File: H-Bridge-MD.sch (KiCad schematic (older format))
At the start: 67 parts, among them IC1 SI8650AB-B-IS1, IC2 A3921KLPTR-T, IC3 SI8650AB-B-IS1, IC4 A3921KLPTR-T, J1 Conn_01x02, J2 Conn_01x03, J3 Conn_01x05, J4 Conn_01x02, J5 Bus_mechaken_PCIexpress_x16_1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, Q1 NVMFD5C446NT1G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

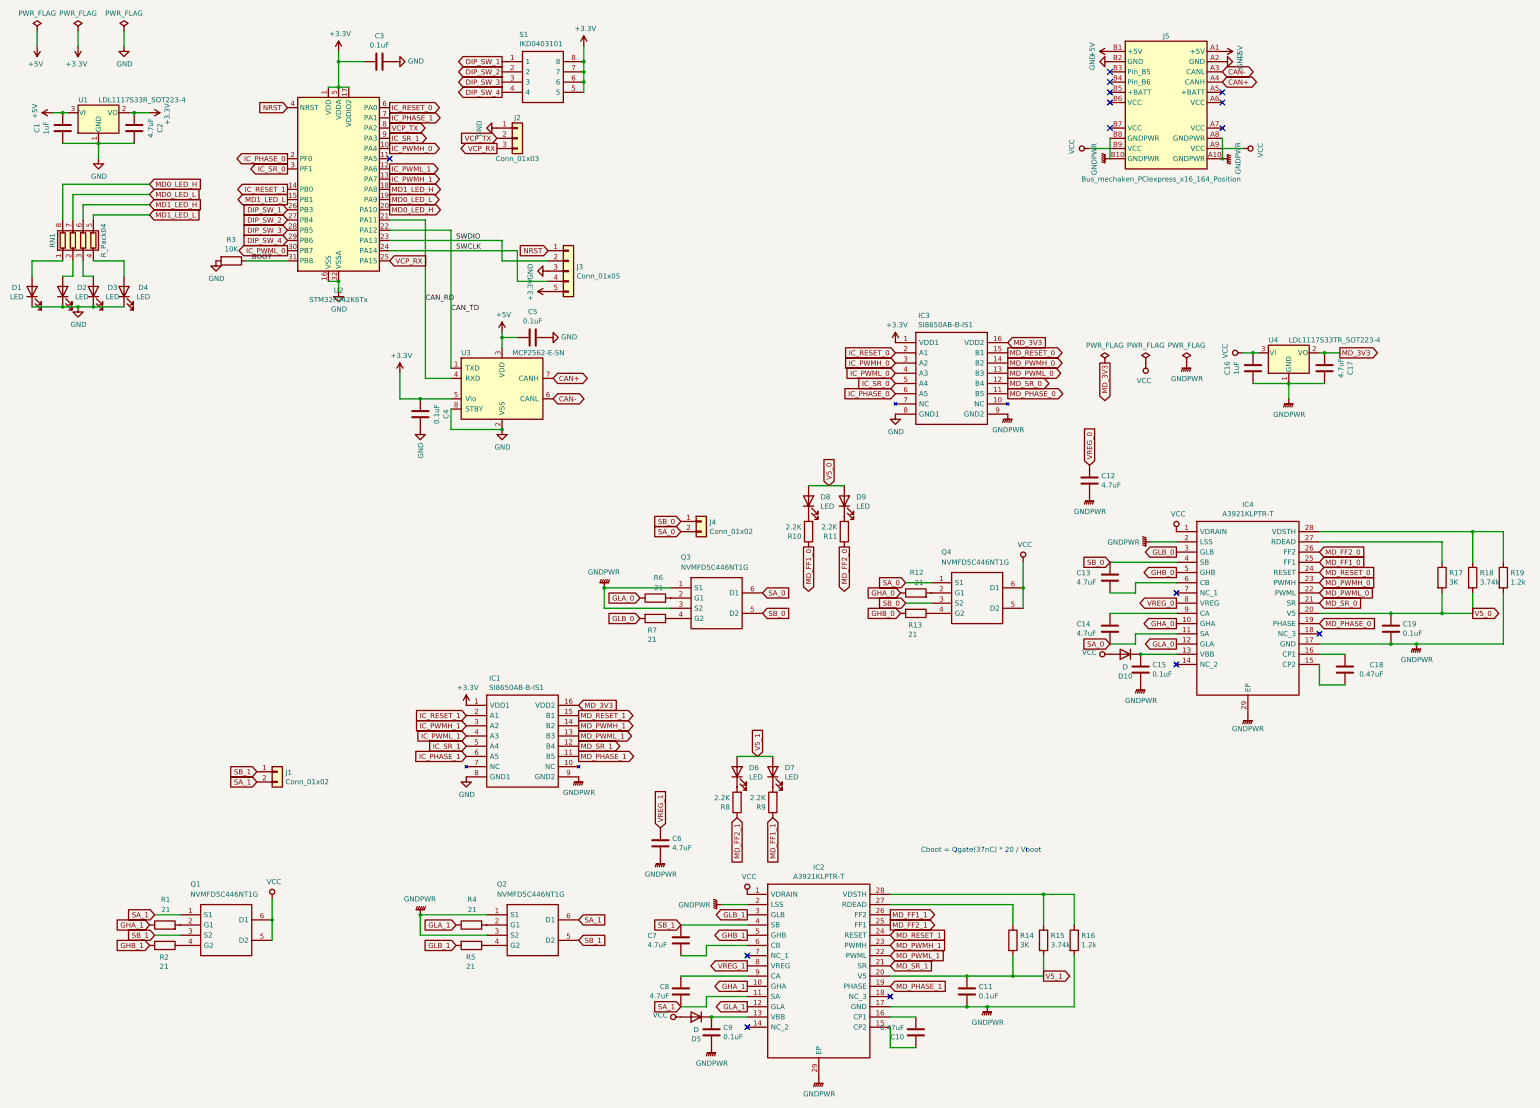
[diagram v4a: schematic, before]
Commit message: change
電解コンデンサを搭載できるように配置を大幅変更
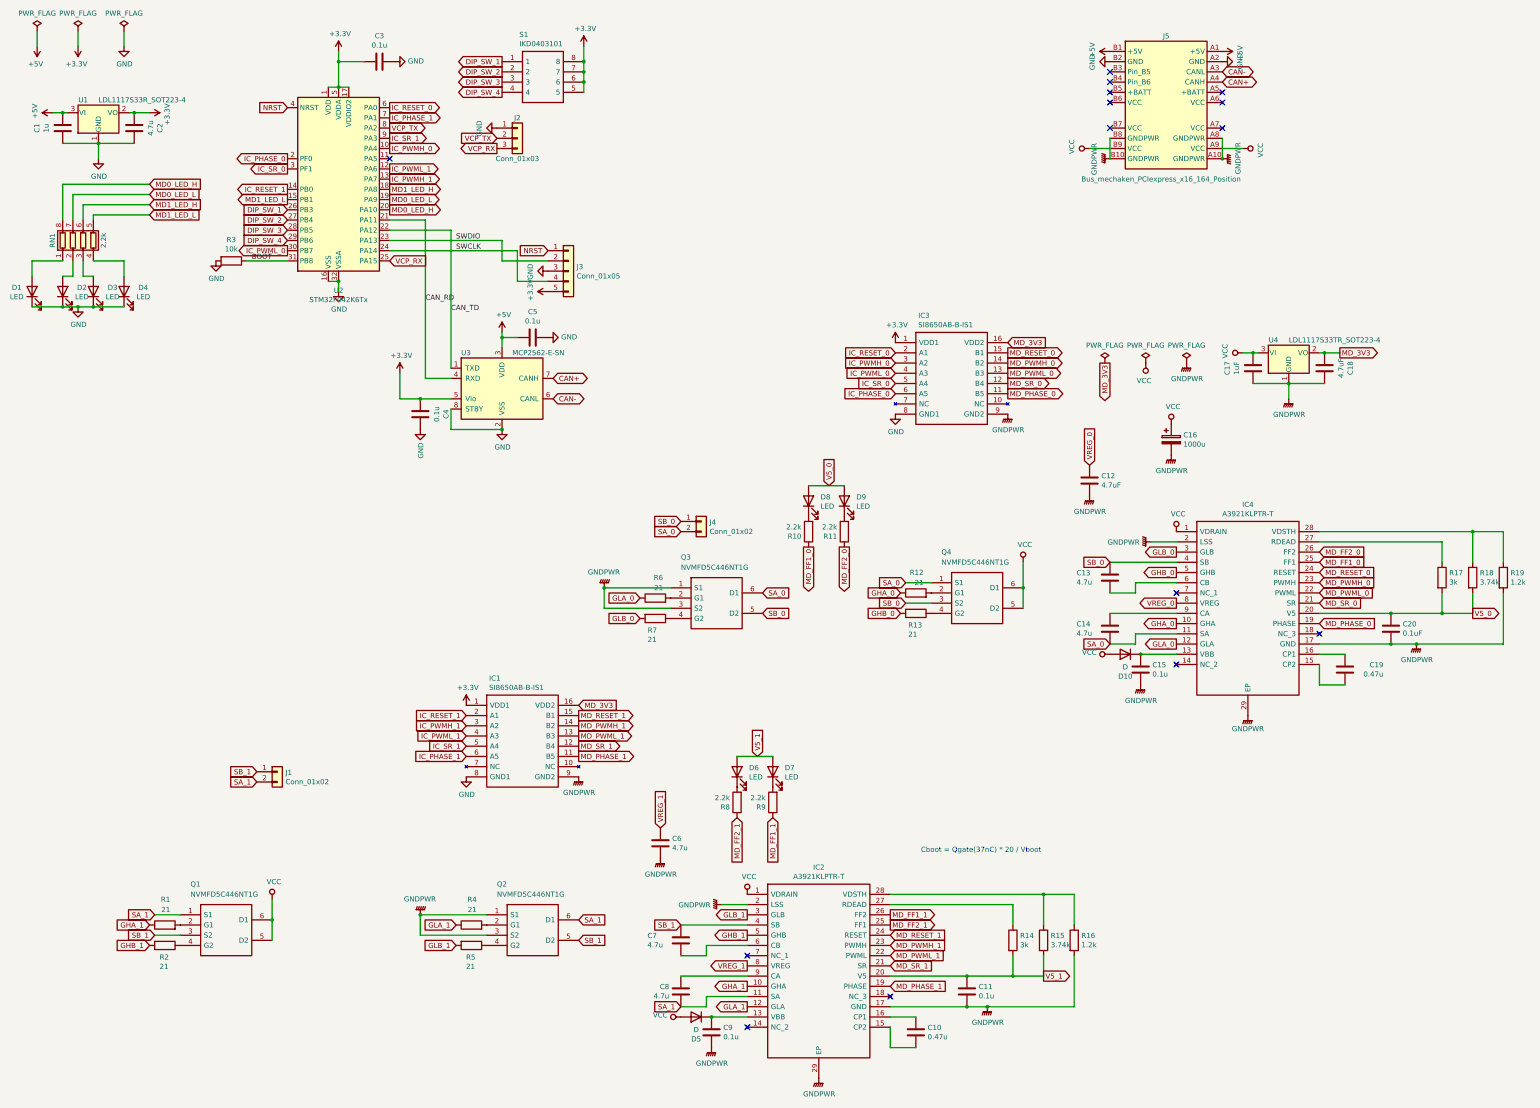
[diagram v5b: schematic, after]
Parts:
- added C16: 1000u, Connector_PinSocket_2.54mm:PinSocket_1x02_P2.54mm_Vertical, symbol Device:CP
- C1: value 1uF -> 1u
- C10: value 0.47uF -> 0.47u
- C11, C15, C3, C4, C5, C9: value 0.1uF -> 0.1u
- C13, C14, C2, C6, C7, C8: value 4.7uF -> 4.7u
- C19: renamed from C18; value 0.47uF -> 0.47u
- R10, R11, R8, R9: value 2.2K -> 2.2k
- R14, R17: value 3K -> 3k
- R3: value 10K -> 10k
- RN1: value R_Pack04 -> 2.2k
- renumbered C16 to C17, C17 to C18, C19 to C20
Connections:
- net GNDPWR: now also C16.2
- net VCC: now also C16.1

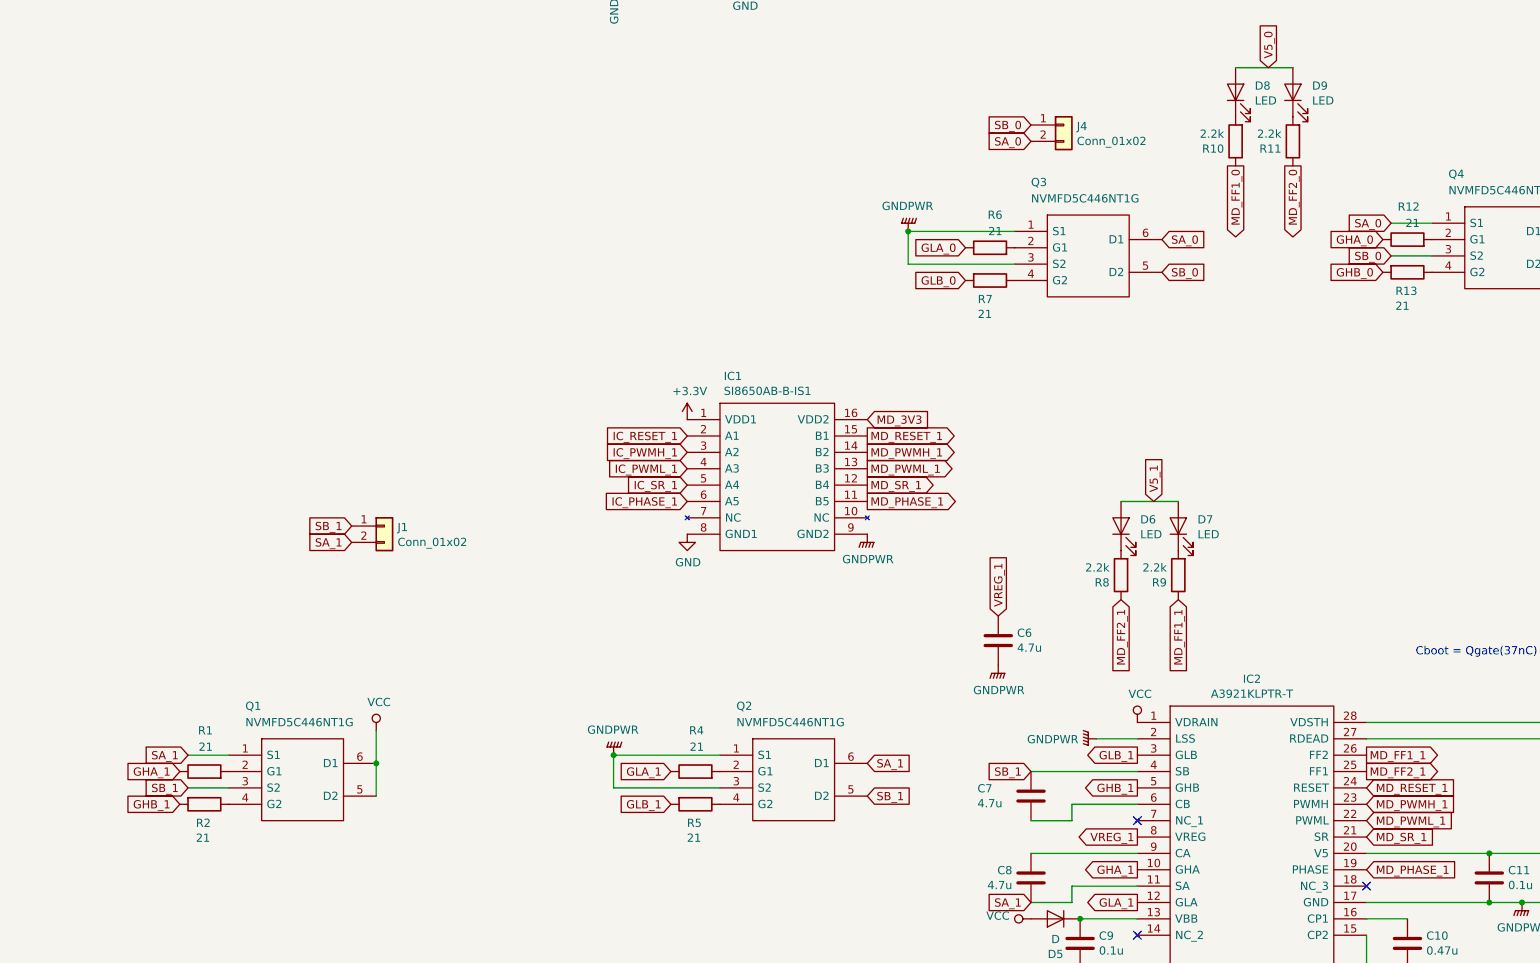
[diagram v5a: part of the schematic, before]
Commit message: change
放熱ビアを1mmに変更
その他大幅な変更
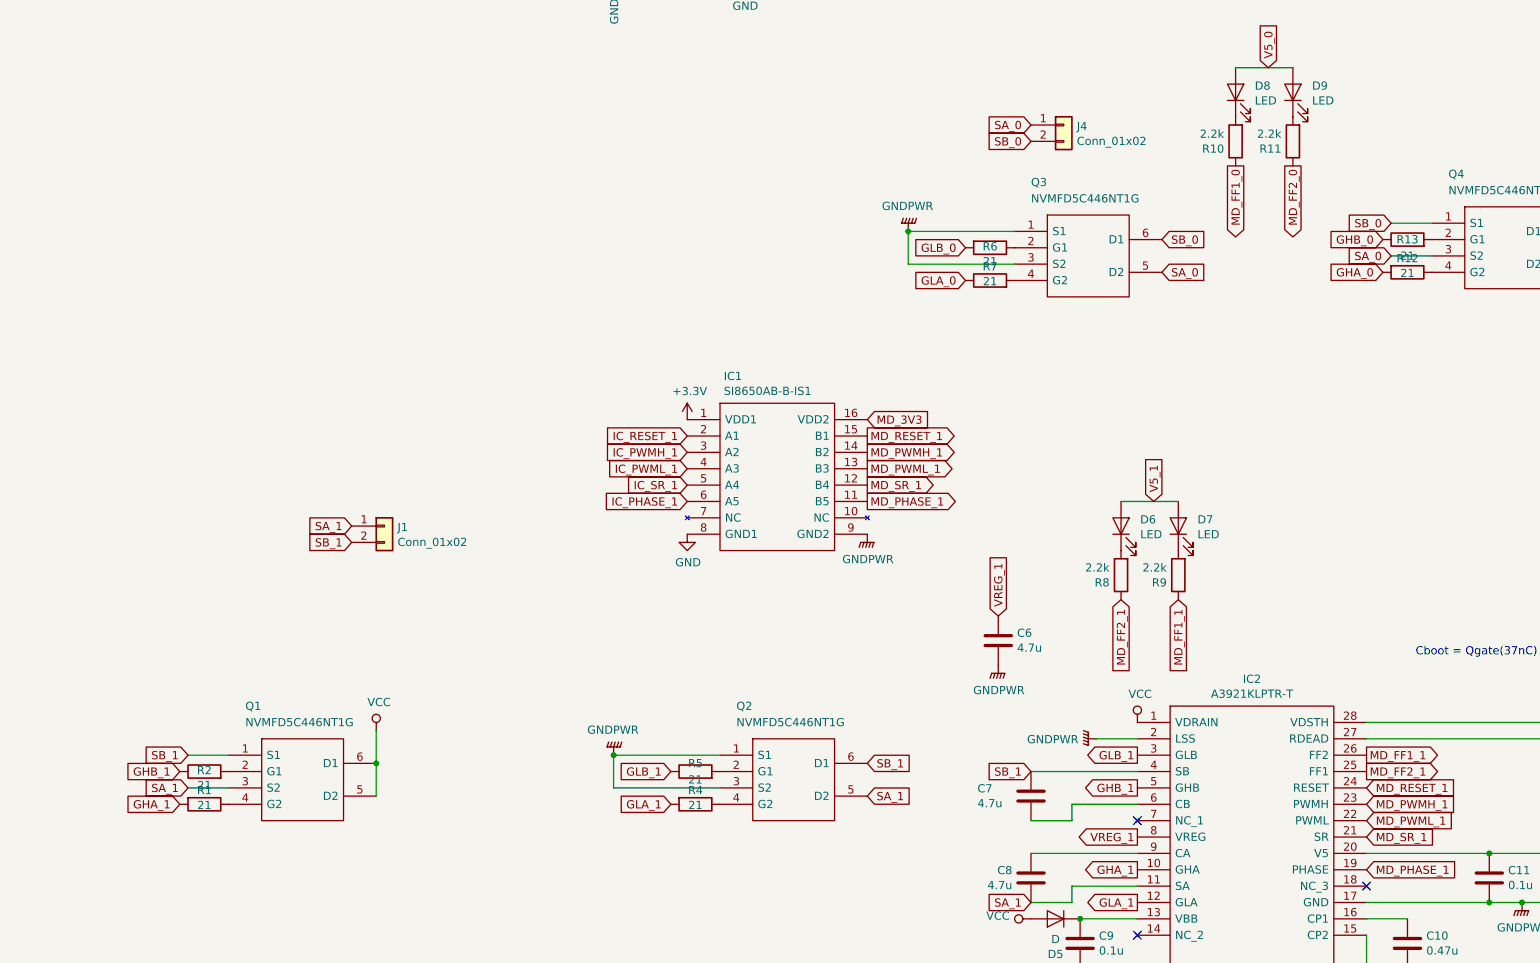
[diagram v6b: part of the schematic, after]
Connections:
- net GHA_0: now also R13.2; no longer R12.1
- net GHA_1: now also R2.2; no longer R1.1
- net GHB_0: now also R12.1; no longer R13.2
- net GHB_1: now also R1.1; no longer R2.2
- net GLA_1: now also R5.2; no longer R4.1
- net GLB_1: now also R4.1; no longer R5.2
- net SA_0: now also J4.1 (Pin_1), Q3.5 (D2), Q4.3 (S2); no longer J4.2 (Pin_2), Q3.6 (D1), Q4.1 (S1)
- net SA_1: now also J1.1 (Pin_1), Q1.3 (S2), Q2.5 (D2); no longer J1.2 (Pin_2), Q1.1 (S1), Q2.6 (D1)
- net SB_0: now also J4.2 (Pin_2), Q3.6 (D1), Q4.1 (S1); no longer J4.1 (Pin_1), Q3.5 (D2), Q4.3 (S2)
- net SB_1: now also J1.2 (Pin_2), Q1.1 (S1), Q2.6 (D1); no longer J1.1 (Pin_1), Q1.3 (S2), Q2.5 (D2)
- net at R6.2: now also Q3.4 (G2); no longer Q3.2 (G1)
- net at R7.1: now also Q3.2 (G1); no longer Q3.4 (G2)
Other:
- moved on the sheet: R6, R7

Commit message: fix
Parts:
- added S2: DIPSW, Package_DIP:DIP-8_W7.62mm, symbol SamacSys_Parts:IKD0403101
- R15, R18: value 3.74k -> 10k
- R16, R19: value 1.2k -> 2.2k
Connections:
- net +3V3: now also S2.5, S2.6, S2.7, S2.8
- net DIP_SW_1: now also S2.4
- net DIP_SW_2: now also S2.3
- net DIP_SW_3: now also S2.2
- net DIP_SW_4: now also S2.1
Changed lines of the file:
@@
 P 15100 6200
 F 0 "R19" H 15170 6246 50  0000 L CNN
-F 1 "1.2k" H 15170 6155 50  0000 L CNN
+F 1 "2.2k" H 15170 6155 50  0000 L CNN
 F 2 "Resistor_SMD:R_0603_1608Metric" V 15030 6200 50  0001 C CNN
 F 3 "~" H 15100 6200 50  0001 C CNN
@@
 P 14800 6200
 F 0 "R18" H 14870 6246 50  0000 L CNN
-F 1 "3.74k" H 14870 6155 50  0000 L CNN
+F 1 "10k" H 14870 6155 50  0000 L CNN
 F 2 "Resistor_SMD:R_0603_1608Metric" V 14730 6200 50  0001 C CNN
 F 3 "~" H 14800 6200 50  0001 C CNN
@@
 U 1 1 5DA97C08
 P 2000 9800
-F 0 "R2" V 1793 9800 50  0000 C CNN
-F 1 "21" V 1884 9800 50  0000 C CNN
+F 0 "R2" V 2115 9800 50  0000 C CNN
+F 1 "21" V 2206 9800 50  0000 C CNN
 F 2 "Resistor_SMD:R_0603_1608Metric" V 1930 9800 50  0001 C CNN
 F 3 "~" H 2000 9800 50  0001 C CNN
@@
 U 1 1 5DA97BF0
 P 2000 9600
-F 0 "R1" V 1885 9600 50  0000 C CNN
-F 1 "21" V 1794 9600 50  0000 C CNN
+F 0 "R1" V 2250 9600 50  0000 C CNN
+F 1 "21" V 2150 9600 50  0000 C CNN
 F 2 "Resistor_SMD:R_0603_1608Metric" V 1930 9600 50  0001 C CNN
 F 3 "~" H 2000 9600 50  0001 C CNN
@@
 U 1 1 5DC02421
 P 9350 6350
-F 0 "R12" V 9235 6350 50  0000 C CNN
-F 1 "21" V 9144 6350 50  0000 C CNN
+F 0 "R12" V 9550 6350 50  0000 C CNN
+F 1 "21" V 9450 6350 50  0000 C CNN
 F 2 "Resistor_SMD:R_0603_1608Metric" V 9280 6350 50  0001 C CNN
 F 3 "~" H 9350 6350 50  0001 C CNN
@@
 U 1 1 5DC02427
 P 9350 6550
-F 0 "R13" V 9150 6550 50  0000 C CNN
-F 1 "21" V 9250 6550 50  0000 C CNN
+F 0 "R13" V 9465 6550 50  0000 C CNN
+F 1 "21" V 9556 6550 50  0000 C CNN
 F 2 "Resistor_SMD:R_0603_1608Metric" V 9280 6550 50  0001 C CNN
 F 3 "~" H 9350 6550 50  0001 C CNN
@@
 U 1 1 5DC02488
 P 6800 6400
-F 0 "R7" V 6915 6400 50  0000 C CNN
-F 1 "21" V 7006 6400 50  0000 C CNN
+F 0 "R7" V 6550 6400 50  0000 C CNN
+F 1 "21" V 6650 6400 50  0000 C CNN
 F 2 "Resistor_SMD:R_0603_1608Metric" V 6730 6400 50  0001 C CNN
 F 3 "~" H 6800 6400 50  0001 C CNN
@@
 U 1 1 5DA97BEA
 P 5000 9600
-F 0 "R4" V 4885 9600 50  0000 C CNN
-F 1 "21" V 4794 9600 50  0000 C CNN
+F 0 "R4" V 5207 9600 50  0000 C CNN
+F 1 "21" V 5116 9600 50  0000 C CNN
 F 2 "Resistor_SMD:R_0603_1608Metric" V 4930 9600 50  0001 C CNN
 F 3 "~" H 5000 9600 50  0001 C CNN
@@
 U 1 1 5DA97C02
 P 5000 9800
-F 0 "R5" V 4750 9800 50  0000 C CNN
-F 1 "21" V 4850 9800 50  0000 C CNN
+F 0 "R5" V 5115 9800 50  0000 C CNN
+F 1 "21" V 5206 9800 50  0000 C CNN
 F 2 "Resistor_SMD:R_0603_1608Metric" V 4930 9800 50  0001 C CNN
 F 3 "~" H 5000 9800 50  0001 C CNN
@@
 P 10600 9750
 F 0 "R15" H 10670 9796 50  0000 L CNN
-F 1 "3.74k" H 10670 9705 50  0000 L CNN
+F 1 "10k" H 10670 9705 50  0000 L CNN
 F 2 "Resistor_SMD:R_0603_1608Metric" V 10530 9750 50  0001 C CNN
 F 3 "~" H 10600 9750 50  0001 C CNN
@@
 P 10900 9750
 F 0 "R16" H 10970 9796 50  0000 L CNN
-F 1 "1.2k" H 10970 9705 50  0000 L CNN
+F 1 "2.2k" H 10970 9705 50  0000 L CNN
 F 2 "Resistor_SMD:R_0603_1608Metric" V 10830 9750 50  0001 C CNN
 F 3 "~" H 10900 9750 50  0001 C CNN
@@
 U 1 1 5DC0241B
 P 6800 6600
-F 0 "R6" V 7007 6600 50  0000 C CNN
-F 1 "21" V 6916 6600 50  0000 C CNN
+F 0 "R6" V 6685 6600 50  0000 C CNN
+F 1 "21" V 6594 6600 50  0000 C CNN
 F 2 "Resistor_SMD:R_0603_1608Metric" V 6730 6600 50  0001 C CNN
 F 3 "~" H 6800 6600 50  0001 C CNN
@@
 	0    -1   -1   0
 $EndComp
+$Comp
+L power:+3.3V #PWR0101
+U 1 1 5E1B3DD4
+P 7100 1750
+F 0 "#PWR0101" H 7100 1600 50  0001 C CNN
+F 1 "+3.3V" H 7115 1923 50  0000 C CNN
+F 2 "" H 7100 1750 50  0001 C CNN
+F 3 "" H 7100 1750 50  0001 C CNN
+	1    7100 1750
+	1    0    0    -1
+$EndComp
+$Comp
+L SamacSys_Parts:IKD0403101 S2
+U 1 1 5E1B3DE0
+P 6300 1900
+F 0 "S2" H 6469 2165 50  0000 L CNN
+F 1 "DIPSW" H 6469 2074 50  0000 L CNN
+F 2 "Package_DIP:DIP-8_W7.62mm" H 6950 2000 50  0001 L CNN
+F 3 "http://uk.rs-online.com/web/p/products/8772264" H 6950 1900 50  0001 L CNN
+F 4 "4 Way Surface Mount DIP Switch SPST, Raised Actuator Slide Actuator" H 6950 1800 50  0001 L CNN "Description"
+F 5 "3.7" H 6950 1700 50  0001 L CNN "Height"
+F 6 "8772264" H 6950 1600 50  0001 L CNN "RS Part Number"
+F 7 "http://uk.rs-online.com/web/p/products/8772264" H 6950 1500 50  0001 L CNN "RS Price/Stock"
+F 8 "Apem" H 6950 1400 50  0001 L CNN "Manufacturer_Name"
+F 9 "IKD0403101" H 6950 1300 50  0001 L CNN "Manufacturer_Part_Number"
+	1    6300 1900
+	1    0    0    -1
+$EndComp
+Wire Wire Line
+	7100 1750 7100 1900
+Connection ~ 7100 1900
+Wire Wire Line
+	7100 1900 7100 2000
+Connection ~ 7100 2000
+Wire Wire Line
+	7100 2000 7100 2100
+Connection ~ 7100 2100
+Wire Wire Line
+	7100 2100 7100 2200
+Text GLabel 6300 2200 0    50   Output ~ 0
+DIP_SW_1
+Text GLabel 6300 2100 0    50   Output ~ 0
+DIP_SW_2
+Text GLabel 6300 2000 0    50   Output ~ 0
+DIP_SW_3
+Text GLabel 6300 1900 0    50   Output ~ 0
+DIP_SW_4
 $EndSCHEMATC
